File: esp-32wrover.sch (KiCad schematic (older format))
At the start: 90 parts, among them CON1 BARREL_JACK, P1 Power, P2 Analog, P3 Digital, P4 Digital, P5 CONN_1, P6 CONN_1, P7 CONN_1, P8 CONN_1, P9 CONN_01X04, Q1 12Mhz, Q2 32.768Khz, Q3 Q_NPN_BEC, Q4 Q_NPN_BEC, SW1 SW_PUSH, SW2 SW_PUSH, U1 usb_mini_b, U2 MCP16311-MNY, U3 BD00GA5WEFJ, U4 PL2303HXA, U5 MCP6001R, U6 ESP32-WROVER, U7 IRLM6402

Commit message: add netlist
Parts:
- gave numbers to parts that had none: 22

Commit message: edit netlist, create pcb
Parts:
- C1, C11, C12, C13, C14, C15, C16, C17, C18, C19, C20, C3, C5, C6, C7, C8, C9: footprint 0603_N -> Capacitors_SMD:C_0603
- C10, C21: footprint 0603_N -> Capacitors_SMD:C_0805
- C2, C4: footprint 0603_N -> Capacitors_SMD:c_elec_5x5.3
- CON1: footprint (none) -> Connect:JACK_ALIM
- D1, D3: footprint (none) -> Diodes_SMD:D_0805
- D10, D11, D6, D7, D8, D9: footprint (none) -> Diodes_SMD:D_0603
- D2, D4, D5: footprint (none) -> LEDs:LED_0603
- L1: footprint (none) -> Inductors:SELF-WE-PD-XXL
- P9: footprint (none) -> Pin_Headers:Pin_Header_Straight_1x04_Pitch1.27mm
- Q1: footprint (none) -> Crystals:Q_49U3HMS
- Q2: footprint (none) -> Crystals:Crystal_SMD_Micro-Crystal_MS1V-T1K
- Q3, Q4, U7: footprint (none) -> TO_SOT_Packages_SMD:SOT-23
- R1, R10, R11, R12, R13, R14, R15, R16, R17, R18, R19, R2, R20, R21, R22, R23, R24, R25, R26, R27, R28, R29, R3, R30, R31, R32, R33, R34, R4, R5, R6, R7, R8, R9: footprint 0603_N -> Resistors_SMD:R_0603
- SW1: footprint (none) -> Buttons_Switches_SMD:SW_SPST_B3SL-1022P
- SW2: footprint (none) -> Buttons_Switches_SMD:SW_SPST_REED_CT05-XXXX-G1
- U1: footprint (none) -> Connect:USB_Mini-B
- U2: footprint Housings_DFN_QFN:DFN-8-1EP_3x2mm_Pitch0.5mm -> Housings_SSOP:MSOP-8-1EP_3x3mm_Pitch0.65mm
- U3: footprint (none) -> Housings_SSOP:MSOP-8-1EP_3x3mm_Pitch0.65mm
- U4: footprint (none) -> Housings_SSOP:SSOP-28_5.3x10.2mm_Pitch0.65mm
- U5: footprint (none) -> TO_SOT_Packages_SMD:SOT-23-5
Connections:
- net at U2.1 (Vfb): now also R10.1, R9.2

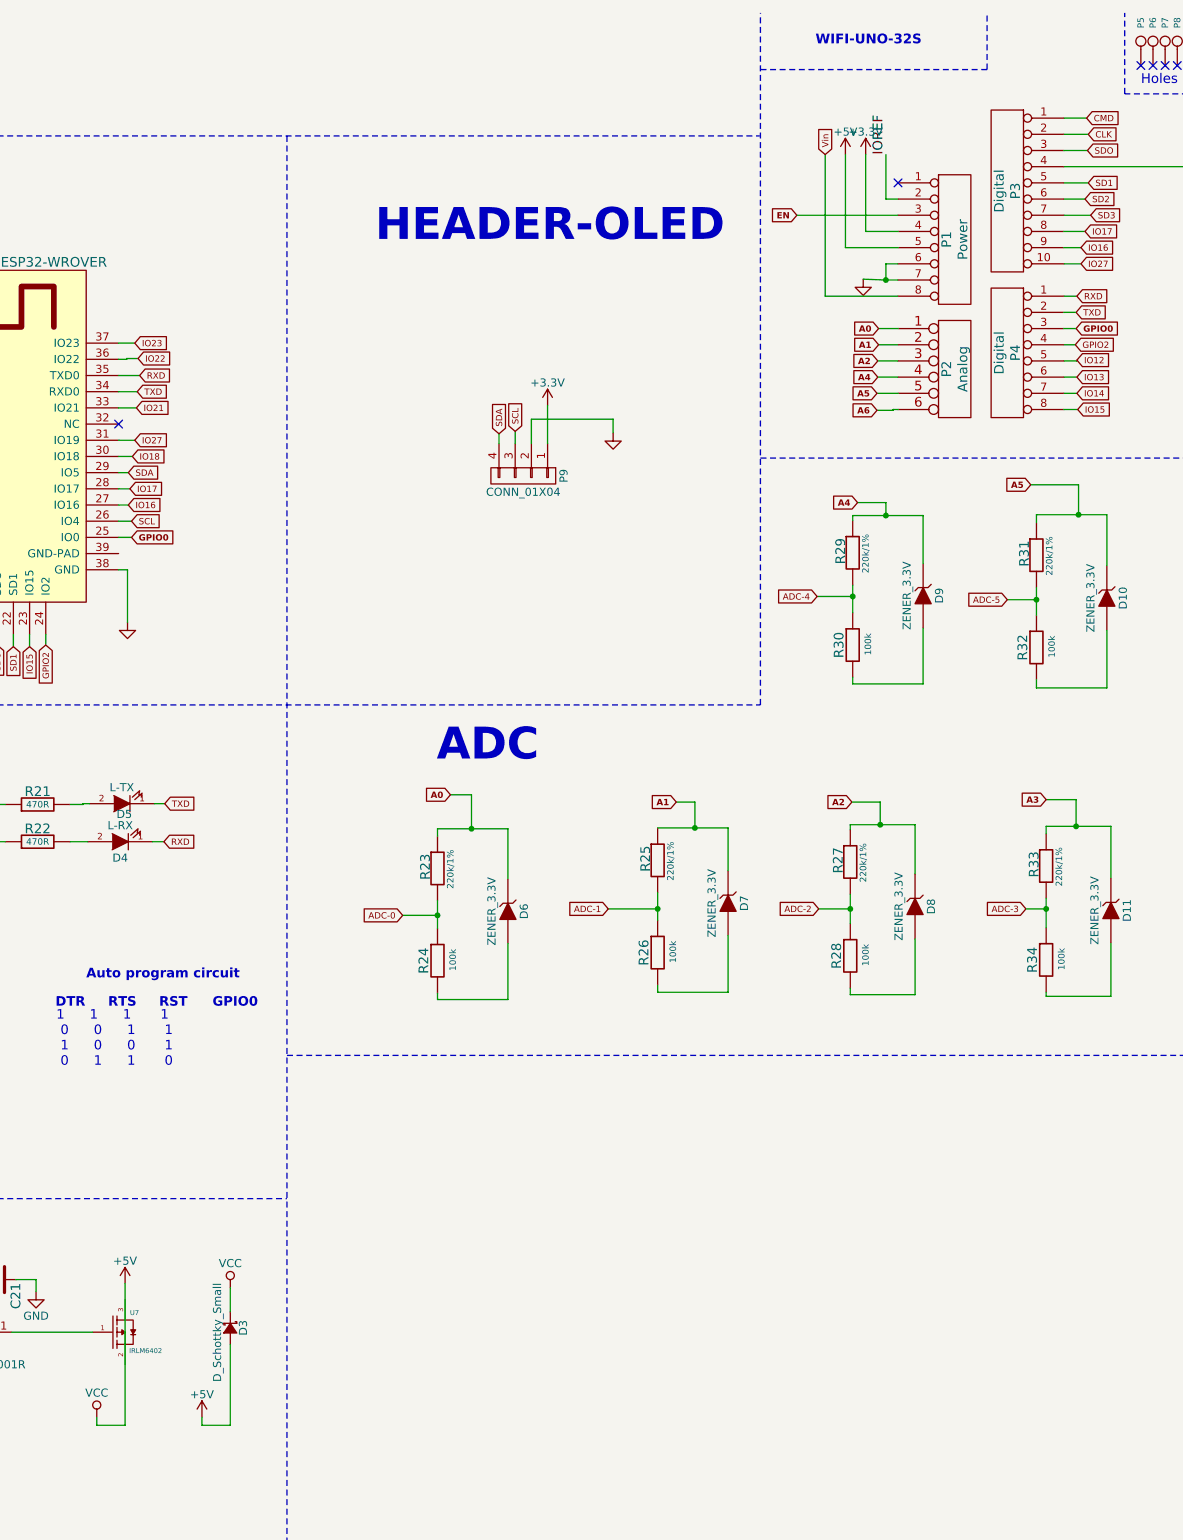
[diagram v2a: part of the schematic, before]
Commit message: thêm header ICSP
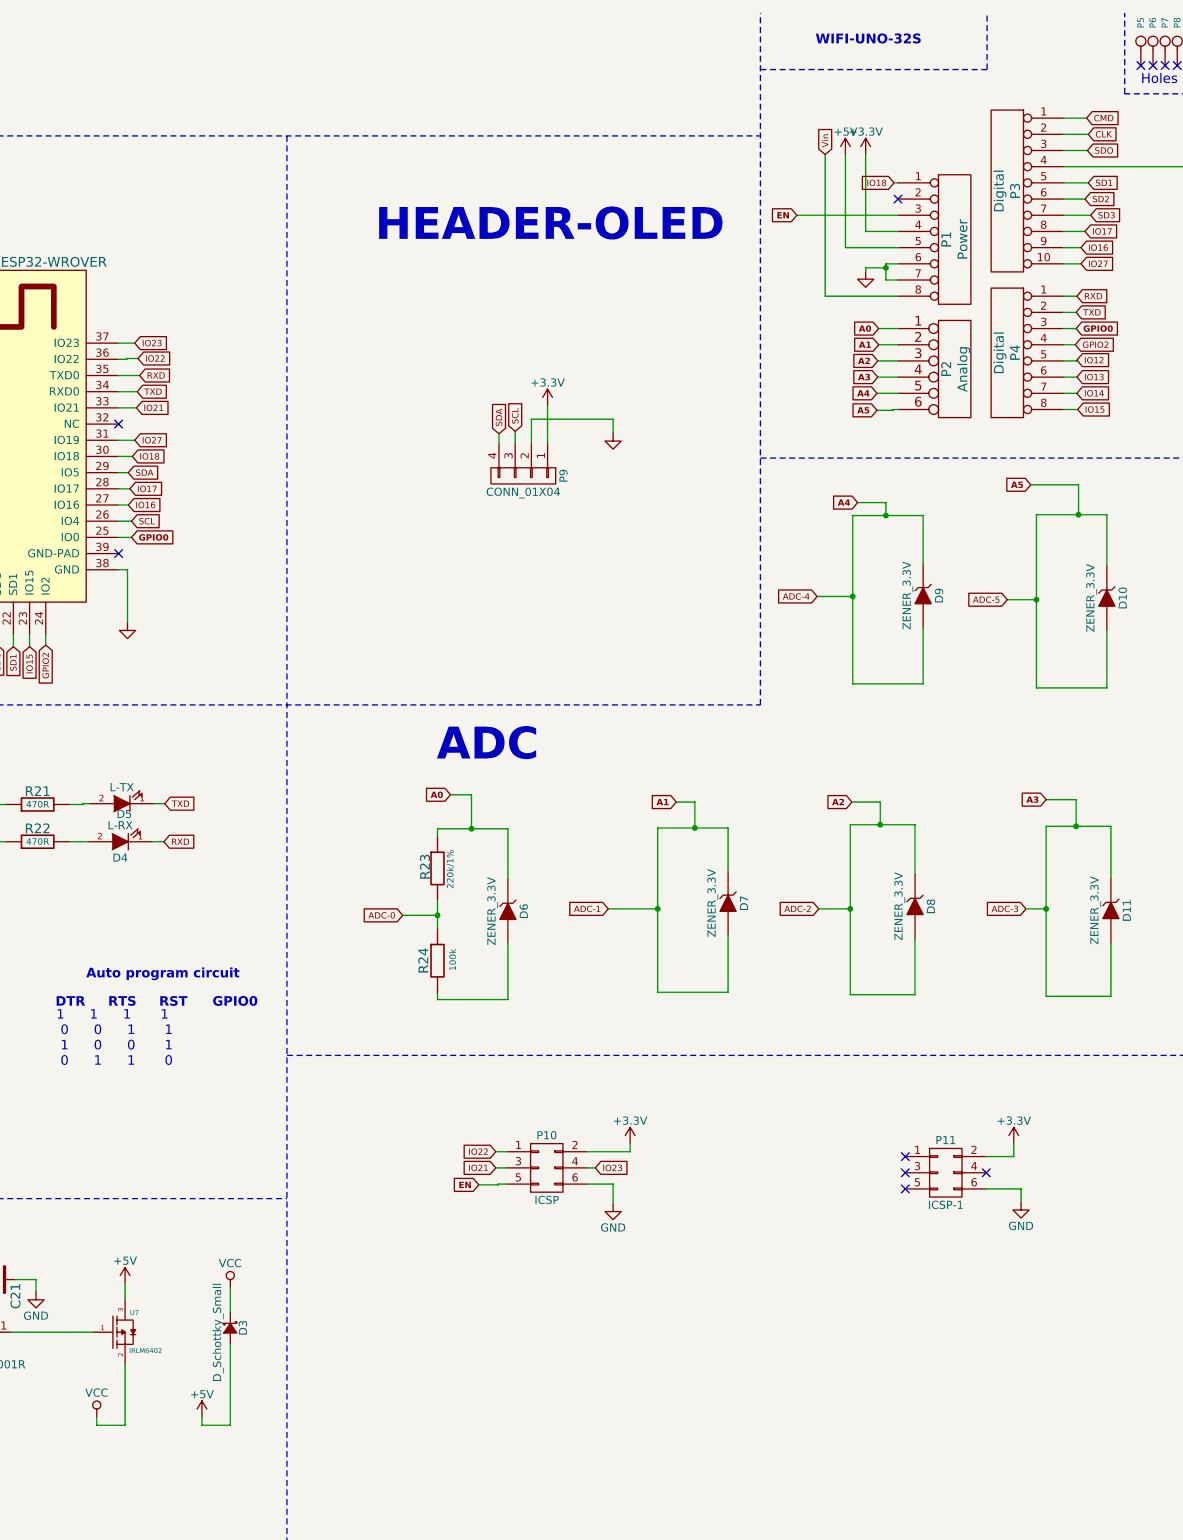
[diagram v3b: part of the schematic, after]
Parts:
- removed R25, R27, R29, R31, R33: 220k/1%, Resistors_SMD:R_0603, symbol R
- removed R26, R28, R30, R32, R34: 100k, Resistors_SMD:R_0603, symbol R
- added P10: ICSP, Pin_Headers:Pin_Header_Straight_2x03_Pitch2.54mm, symbol CONN_02X03
- added P11: ICSP-1, Pin_Headers:Pin_Header_Angled_2x03_Pitch2.54mm, symbol CONN_02X03
- L1: footprint Inductors:SELF-WE-PD-XXL -> Inductors:SELF-WE-TPC_M
- SW1: footprint Buttons_Switches_SMD:SW_SPST_B3SL-1022P -> Buttons_Switches_SMD:SW_SPST_REED_CT05-XXXX-G1
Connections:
- net A6 is gone; now on net A5: P2.6
- net ADC-1 is gone; now on net A1: U6.5 (SENSOR_VN)
- net ADC-2 is gone; now on net A2: U6.6 (IO34)
- net ADC-3 is gone; now on net A3: U6.7 (IO35)
- net ADC-4 is gone; now on net A4: U6.10 (IO25)
- net ADC-5 is gone; now on net A5: U6.11 (IO26)
- net +3V3: now also P10.2 (P2), P11.2 (P2)
- net +5V: now also U7.3; no longer C19.2, C5.2, D3.1 (K), U1.1 (VBUS), U4.20 (VDD_5V)
- net A1: now also D7.2 (A)
- net A2: now also D8.2 (A)
- net A3: now also D11.2 (A), P2.4
- net A4: now also D9.2 (A), P2.5; no longer P2.4
- net A5: now also D10.2 (A); no longer P2.5
- net EN: now also P10.5 (P5)
- net GND: now also P10.6 (P6), P11.6 (P6)
- net IO18: now also P1.1 (P1)
- net IO21: now also P10.3 (P3)
- net IO22: now also P10.1 (P1)
- net IO23: now also P10.4 (P4)
- net VCC: now reaches U7.2
- net VCC: now also C19.2, C5.2, D3.1 (K), U1.1 (VBUS), U4.20 (VDD_5V)
- net IOREF: no longer names the net of P1.2 (P2)
- no-connect marks 18 -> 23

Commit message: sap xep linh kien
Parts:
- removed Q1: 12Mhz, Crystals:Q_49U3HMS, symbol XT_2pin
- removed Q2: 32.768Khz, Crystals:Crystal_SMD_Micro-Crystal_MS1V-T1K, symbol XT_2pin
- removed R23: 220k/1%, Resistors_SMD:R_0603, symbol R
- removed R24: 100k, Resistors_SMD:R_0603, symbol R
- added Y1: 12Mhz, symbol Crystal
- added Y2: 32.768Khz, symbol Crystal
- D1, D3: value D_Schottky_Small -> SS24
- P11: footprint Pin_Headers:Pin_Header_Angled_2x03_Pitch2.54mm -> Pin_Headers:Pin_Header_Straight_2x03_Pitch2.54mm
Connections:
- net A1: no longer D7.2 (A), U6.5 (SENSOR_VN)
- net A2: no longer D8.2 (A), U6.6 (IO34)
- net A3: no longer D11.2 (A), U6.7 (IO35)
- net A4: no longer D9.2 (A), U6.10 (IO25)
- net A5: no longer D10.2 (A), U6.11 (IO26)
- net ADC-0: now also D6.2 (A)
- net GND: now also CON1.2
- net GPIO0: now also P4.1 (P1); no longer P4.3 (P3)
- net GPIO2: now also P4.2 (P2); no longer P4.4 (P4)
- net IO12: now also P4.3 (P3); no longer P4.5 (P5)
- net IO13: now also P4.4 (P4); no longer P4.6 (P6)
- net IO14: now also P4.5 (P5); no longer P4.7 (P7)
- net IO15: now also P4.6 (P6); no longer P4.8 (P8)
- net RXD: now also P4.8 (P8); no longer P4.1 (P1)
- net TXD: now also P4.7 (P7); no longer P4.2 (P2)
- net at C14.1, U6.8 (IO32): now also Y2.1
- net at C13.1, U6.9 (IO33): now also Y2.2
- net at C8.1, U4.28 (OSC2): now also Y1.1
- net at C7.1, U4.27 (OSC1): now also Y1.2
- new net ADC-1: D7.2 (A), U6.5 (SENSOR_VN)
- new net ADC-2: D8.2 (A), U6.6 (IO34)
- new net ADC-3: D11.2 (A), U6.7 (IO35)
- new net ADC-4: D9.2 (A), U6.10 (IO25)
- new net ADC-5: D10.2 (A), U6.11 (IO26)
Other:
- moved on the sheet: D10, D11, D6, D7, D8, D9

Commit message: đi dây PCB
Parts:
- removed P11: ICSP-1, Pin_Headers:Pin_Header_Straight_2x03_Pitch2.54mm, symbol CONN_02X03
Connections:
- net CLK: now also P3.3 (P3); no longer P3.2 (P2)
- net CMD: now also P3.5 (P5); no longer P3.1 (P1)
- net GPIO0: now also P4.4 (P4); no longer P4.1 (P1)
- net GPIO2: now also P4.3 (P3); no longer P4.2 (P2)
- net IO12: now also P3.9 (P9); no longer P4.3 (P3)
- net IO13: now also P3.8 (P8); no longer P4.4 (P4)
- net IO14: now also P3.10 (P10); no longer P4.5 (P5)
- net IO15: now also P4.2 (P2); no longer P4.6 (P6)
- net IO16: now also P4.5 (P5); no longer P3.9 (P9)
- net IO17: now also P4.6 (P6); no longer P3.8 (P8)
- net IO27: now also P4.1 (P1); no longer P3.10 (P10), U6.31 (IO19)
- net SD1: now also P3.1 (P1); no longer P3.5 (P5)
- net SD2: now also P3.7 (P7); no longer P3.6 (P6)
- net SD3: now also P3.6 (P6); no longer P3.7 (P7)
- net SDO: now also P3.2 (P2); no longer P3.3 (P3)
- net IO18: no longer names the net of P1.1 (P1)
- net IO18: no longer U6.30 (IO18)
- no-connect marks 23 -> 25
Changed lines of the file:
@@
 $EndDescr
-$Comp
-L CONN_8 P1
-U 1 1 5517C2C1
-P 14525 1875
-F 0 "P1" V 14475 1875 60  0000 C CNN
-F 1 "Power" V 14575 1875 60  0000 C CNN
-F 2 "Socket_Arduino_Uno:Socket_Strip_Arduino_1x08" H 14525 1875 60  0001 C CNN
-F 3 "" H 14525 1875 60  0000 C CNN
-	1    14525 1875
-	1    0    0    -1
-$EndComp
 $Comp
 L CONN_6 P2
@@
 Text GLabel 9470 2915 2    39   Input ~ 0
 IO21
-Text GLabel 9460 3115 2    39   Input ~ 0
-IO27
-Text GLabel 9445 3215 2    39   Input ~ 0
-IO18
 Text GLabel 9430 3415 2    39   Input ~ 0
 IO17
@@
 Text GLabel 15285 2925 2    39   Input ~ 0
 RXD
+Text GLabel 15305 1925 2    39   Input ~ 0
+IO12
+Text GLabel 15305 2025 2    39   Input ~ 0
+IO14
+Text GLabel 15280 2225 2    39   Input ~ 0
+IO27
+Text GLabel 15280 2725 2    39   Input ~ 0
+IO17
+Text GLabel 15280 2625 2    39   Input ~ 0
+IO16
+Text GLabel 15270 2525 2    39   Input ~ 8
+GPIO0
 Text GLabel 15275 2425 2    39   Input ~ 0
-IO12
-Text GLabel 15280 2625 2    39   Input ~ 0
-IO14
-Text GLabel 15305 2025 2    39   Input ~ 0
-IO27
+GPIO2
+Text GLabel 15275 2325 2    39   Input ~ 0
+IO15
+Text GLabel 15365 1725 2    39   Input ~ 0
+SD2
 Text GLabel 15330 1825 2    39   Input ~ 0
-IO17
-Text GLabel 15305 1925 2    39   Input ~ 0
-IO16
-Text GLabel 15280 2225 2    39   Input ~ 8
-GPIO0
-Text GLabel 15275 2325 2    39   Input ~ 0
-GPIO2
-Text GLabel 15280 2725 2    39   Input ~ 0
-IO15
+IO13
 Text GLabel 15330 1625 2    39   Input ~ 0
-SD2
-Text GLabel 15270 2525 2    39   Input ~ 0
-IO13
-Text GLabel 15365 1725 2    39   Input ~ 0
 SD3
+Text GLabel 15350 1525 2    39   Input ~ 0
+CMD
+Text GLabel 15345 1325 2    39   Input ~ 0
+CLK
+Text GLabel 15350 1225 2    39   Input ~ 0
+SDO
 Text GLabel 15340 1125 2    39   Input ~ 0
-CMD
-Text GLabel 15350 1225 2    39   Input ~ 0
-CLK
-Text GLabel 15345 1325 2    39   Input ~ 0
-SDO
-Text GLabel 15350 1525 2    39   Input ~ 0
 SD1
 NoConn ~ 5965 6650
@@
 NoConn ~ 14175 1625
 NoConn ~ 9360 3815
-Text GLabel 14150 1525 0    39   Input ~ 0
-IO18
 Wire Wire Line
 	13975 1825 14175 1825
@@
 	9430 3415 9360 3415
 Wire Wire Line
-	9445 3215 9360 3215
-Wire Wire Line
-	9460 3115 9360 3115
-Wire Wire Line
 	9470 2915 9360 2915
 Wire Wire Line
@@
 	9400 8825 9400 9200
 Wire Wire Line
-	14175 1525 14150 1525
-Wire Wire Line
 	14100 2025 14100 2125
 Wire Wire Line
@@
 	13975 2050 13975 2070
 Connection ~ 14100 2050
-$Comp
-L CONN_02X03 P11
-U 1 1 587C01FD
-P 14470 7640
-F 0 "P11" H 14470 7840 50  0000 C CNN
-F 1 "ICSP-1" H 14470 7440 50  0000 C CNN
-F 2 "Pin_Headers:Pin_Header_Straight_2x03_Pitch2.54mm" H 14470 6440 50  0001 C CNN
-F 3 "" H 14470 6440 50  0000 C CNN
-	1    14470 7640
-	1    0    0    -1
-$EndComp
-$Comp
-L +3.3V #PWR042
-U 1 1 587FE302
-P 14890 7460
-F 0 "#PWR042" H 14890 7310 50  0001 C CNN
-F 1 "+3.3V" H 14890 7600 50  0000 C CNN
-F 2 "" H 14890 7460 60  0000 C CNN
-F 3 "" H 14890 7460 60  0000 C CNN
-	1    14890 7460
-	1    0    0    -1
-$EndComp
-$Comp
-L GND #PWR043
-U 1 1 587FE421
-P 14935 7820
-F 0 "#PWR043" H 14935 7570 50  0001 C CNN
-F 1 "GND" H 14935 7670 50  0000 C CNN
-F 2 "" H 14935 7820 60  0000 C CNN
-F 3 "" H 14935 7820 60  0000 C CNN
-	1    14935 7820
-	1    0    0    -1
-$EndComp
-Wire Wire Line
-	14720 7540 14890 7540
-Wire Wire Line
-	14890 7540 14890 7460
-Wire Wire Line
-	14720 7740 14935 7740
-Wire Wire Line
-	14935 7740 14935 7820
-NoConn ~ 14720 7640
-NoConn ~ 14220 7740
-NoConn ~ 14220 7640
-NoConn ~ 14220 7540
 $Comp
 L Crystal Y2
@@
 Wire Wire Line
 	15165 4200 14975 4200
+$Comp
+L CONN_8 P1
+U 1 1 5517C2C1
+P 14525 1875
+F 0 "P1" V 14475 1875 60  0000 C CNN
+F 1 "Power" V 14575 1875 60  0000 C CNN
+F 2 "Socket_Arduino_Uno:Socket_Strip_Arduino_1x08" H 14525 1875 60  0001 C CNN
+F 3 "" H 14525 1875 60  0000 C CNN
+	1    14525 1875
+	1    0    0    -1
+$EndComp
+NoConn ~ 14175 1525
+NoConn ~ 9360 3215
+NoConn ~ 9360 3115
+NoConn ~ 13115 1565
+NoConn ~ 17705 1915
+NoConn ~ 16270 1850
 $EndSCHEMATC

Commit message: sắp xếp linh kiện, đi dây
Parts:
- removed P1: Power, Socket_Arduino_Uno:Socket_Strip_Arduino_1x08, symbol CONN_8
- removed Y1: 12Mhz, symbol Crystal
- added C3: 33pF, Capacitors_SMD:C_0603, symbol C
- added D2: L-RST, LEDs:LED_0603, symbol LED
- added P3: Analog, new:Socket_Strip_Arduino_1x06, symbol CONN_6
- added X1: CRYSTAL_ABM3C, Crystals:Crystal_SMD_5032-4pin_5.0x3.2mm, symbol CRYSTAL_ABM3C
- C18: renamed from C16; footprint Capacitors_SMD:C_0603 -> Capacitors_SMD:C_0805
- C20: renamed from C17; footprint Capacitors_SMD:C_0603 -> Capacitors_SMD:C_0805
- C4: renamed from C2; footprint Capacitors_SMD:c_elec_5x5.3 -> Capacitors_SMD:C_1210
- C6: renamed from C4; footprint Capacitors_SMD:c_elec_5x5.3 -> Capacitors_SMD:C_1210
- P1: renamed from P9; footprint Pin_Headers:Pin_Header_Straight_1x04_Pitch1.27mm -> Pin_Headers:Pin_Header_Straight_1x04_Pitch2.54mm
- P10: renamed from P8; footprint Socket_Arduino_Uno:Arduino_1pin -> new:Arduino_1pin
- P4: renamed from P2; footprint Socket_Arduino_Uno:Socket_Strip_Arduino_1x06 -> new:Socket_Strip_Arduino_1x06
- P5: renamed from P3; footprint Socket_Arduino_Uno:Socket_Strip_Arduino_1x10 -> new:Socket_Strip_Arduino_1x10
- P6: renamed from P4; footprint Socket_Arduino_Uno:Socket_Strip_Arduino_1x08 -> new:Socket_Strip_Arduino_1x08
- P7: renamed from P5; footprint Socket_Arduino_Uno:Arduino_1pin -> new:Arduino_1pin
- P8: renamed from P6; footprint Socket_Arduino_Uno:Arduino_1pin -> new:Arduino_1pin
- P9: renamed from P7; footprint Socket_Arduino_Uno:Arduino_1pin -> new:Arduino_1pin
- SW1, SW2: footprint Buttons_Switches_SMD:SW_SPST_REED_CT05-XXXX-G1 -> Buttons_Switches_SMD:SW_SPST_EVQPE1
- U6: footprint ESP32-footprints-Lib:ESP32-WROOM -> new:esp32-wrover
- Y1: renamed from Y2; footprint (none) -> Crystals:Crystal_DS26_d2.0mm_l6.0mm_Horizontal
- renumbered C9 to C10, C10 to C11, C11 to C12, C12 to C13, C13 to C14, C14 to C15, C15 to C16, C19 to C17, C20 to C19, C5 to C2, C18 to C21, C21 to C22, C3 to C5, C8 to C7, C6 to C8, C7 to C9, D9 to D10, D10 to D11, D11 to D12, D2 to D3, D3 to D6, D6 to D7, D7 to D8, D8 to D9, P10 to P2, Q3 to Q1, Q4 to Q2, R13 to R11, R14 to R12, R15 to R13, R11 to R14, R12 to R15, R19 to R16, R20 to R17, R16 to R18, R17 to R19, R3 to R2, R18 to R20, R2 to R3, U4 to U3, U3 to U4
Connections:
- net +3V3: now also C3.2, D2.2 (A), P3.2
- net +5V: now also P3.3
- net ADC-0: now also U6.11 (IO26); no longer U6.4 (SENSOR_VP)
- net ADC-1: now also U6.10 (IO25); no longer U6.5 (SENSOR_VN)
- net ADC-2: now also U6.7 (IO35); no longer U6.6 (IO34)
- net ADC-3: now also U6.6 (IO34); no longer U6.7 (IO35)
- net ADC-4: now also U6.5 (SENSOR_VN); no longer U6.10 (IO25)
- net ADC-5: now also U6.4 (SENSOR_VP); no longer U6.11 (IO26)
- net CLK: now also P5.1 (P1); no longer P5.3 (P3)
- net EN: now also C5.1, R3.2, SW2.2, P3.1; no longer R3.1
- net GND: now also C3.1, P3.4, P3.5, X1.2 (GND), X1.4 (GND)
- net SD1: now also P5.3 (P3); no longer P5.1 (P1)
- net Vin: now also P3.6
- net at C9.1: now also U3.28 (OSC2), X1.3; no longer U3.27 (OSC1)
- net at C7.1: now also U3.27 (OSC1), X1.1; no longer U3.28 (OSC2)
- new net: D2.1 (K), R3.1
- no-connect marks 25 -> 23
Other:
- note added: "ICSP\n"
- moved on the sheet: C7, C9, R3
